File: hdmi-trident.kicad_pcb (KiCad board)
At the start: 4 copper layers, 34.5 x 48 mm, 7 parts, among them J1 HDMI_A_1.4, J2 HDMI_A_1.4, J3 Conn_02x06_Odd_Even, J4 Conn_01x06, J5 HDMI_A_1.4

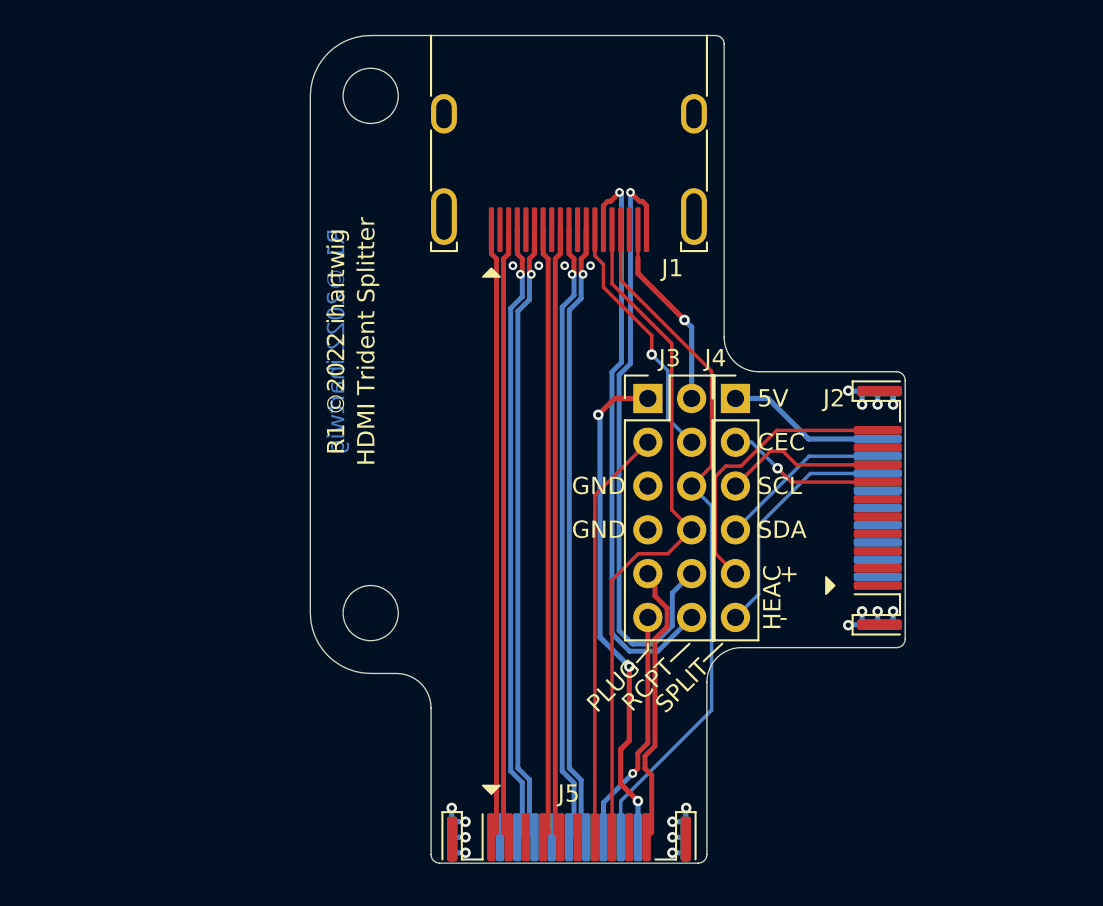
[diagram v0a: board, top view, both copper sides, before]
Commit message: change rcpt to vertical smt w/ new board shape
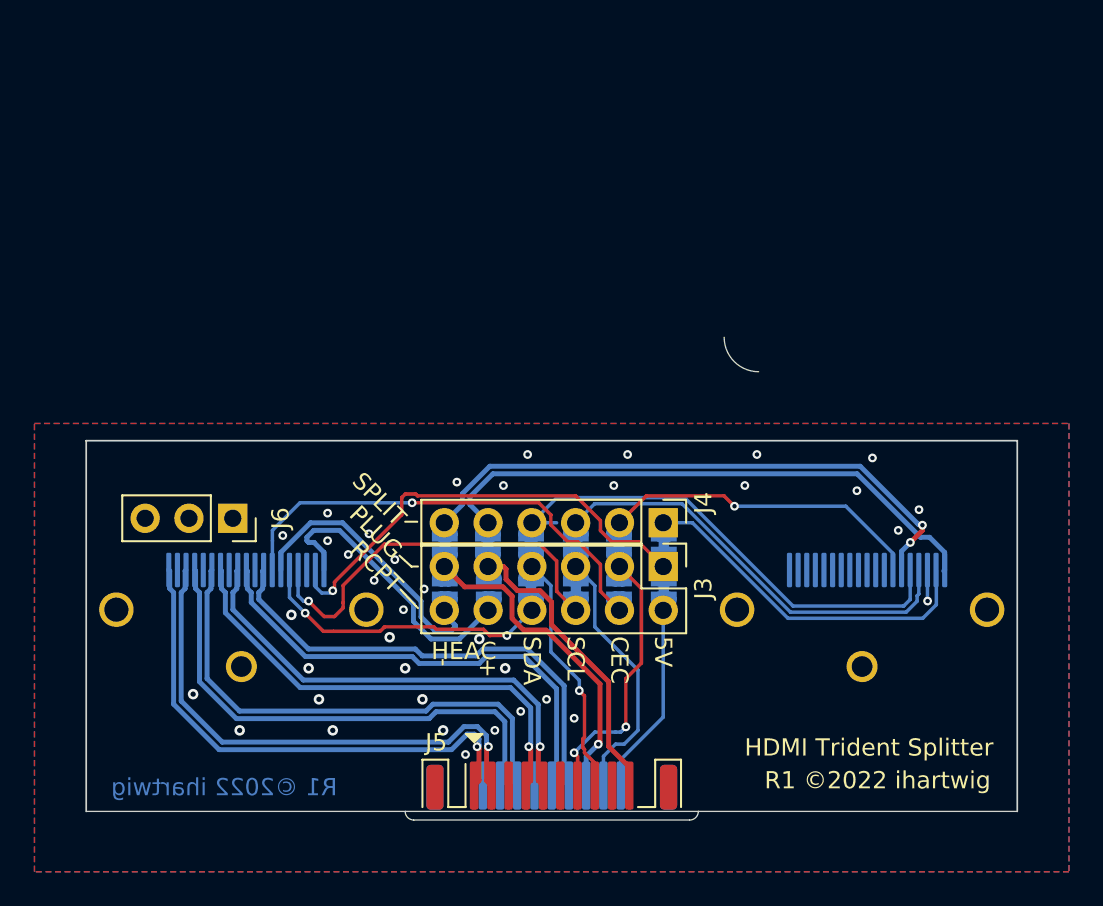
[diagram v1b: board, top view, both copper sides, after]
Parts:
- removed REF** (x2): MountingHole_3.2mm_M3_DIN965, MountingHole:MountingHole_3.2mm_M3_DIN965
- added J6: Conn_01x03, Connector_PinSocket_2.54mm:PinSocket_1x03_P2.54mm_Vertical, F.Cu at (131.5, 89.5)
- added JP1: SolderJumper_2_Bridged, Jumper:SolderJumper-2_P1.3mm_Bridged_RoundedPad1.0x1.5mm, B.Cu at (156.5, 93.6)
- added JP10: SolderJumper_2_Open, Jumper:SolderJumper-2_P1.3mm_Open_RoundedPad1.0x1.5mm, B.Cu at (151.4, 91.0)
- added JP11: SolderJumper_2_Bridged, Jumper:SolderJumper-2_P1.3mm_Bridged_RoundedPad1.0x1.5mm, B.Cu at (146.3, 91.0)
- added JP12: SolderJumper_2_Bridged, Jumper:SolderJumper-2_P1.3mm_Bridged_RoundedPad1.0x1.5mm, B.Cu at (143.8, 91.0)
- added JP2: SolderJumper_2_Open, Jumper:SolderJumper-2_P1.3mm_Open_RoundedPad1.0x1.5mm, B.Cu at (153.9, 93.6)
- added JP3: SolderJumper_2_Bridged, Jumper:SolderJumper-2_P1.3mm_Bridged_RoundedPad1.0x1.5mm, B.Cu at (151.4, 93.6)
- added JP4: SolderJumper_2_Bridged, Jumper:SolderJumper-2_P1.3mm_Bridged_RoundedPad1.0x1.5mm, B.Cu at (148.8, 93.6)
- added JP5: SolderJumper_2_Open, Jumper:SolderJumper-2_P1.3mm_Open_RoundedPad1.0x1.5mm, B.Cu at (146.3, 93.6)
- added JP6: SolderJumper_2_Open, Jumper:SolderJumper-2_P1.3mm_Open_RoundedPad1.0x1.5mm, B.Cu at (143.8, 93.6)
- added JP7: SolderJumper_2_Bridged, Jumper:SolderJumper-2_P1.3mm_Bridged_RoundedPad1.0x1.5mm, B.Cu at (156.5, 91.0)
- added JP8: SolderJumper_2_Bridged, Jumper:SolderJumper-2_P1.3mm_Bridged_RoundedPad1.0x1.5mm, B.Cu at (153.9, 91.0)
- added JP9: SolderJumper_2_Open, Jumper:SolderJumper-2_P1.3mm_Open_RoundedPad1.0x1.5mm, B.Cu at (148.8, 91.0)
- J1: footprint hdmi-trident-special:HDMI_A_Rcpt_HD04 -> hdmi-trident-special:HDMI_A_Rcpt_Vert_3Post; moved to B.Cu
- J2: footprint hdmi-trident-special:HDMI_A_Contact_Technology_HDMI-19APL2_Horizontal -> hdmi-trident-special:HDMI_A_Rcpt_Vert_3Post; moved to B.Cu
- J5: footprint hdmi-trident-special:HDMI_A_Contact_Technology_HDMI-19APL2_Horizontal -> hdmi-trident-special:HDMI_A_Plug_Horizontal_EdgeMount
- moved J1 28.0 mm to (132.0, 92.5)
- moved J3 9.79 mm to (156.5, 92.3), turned to -90 degrees
- moved J4 8.34 mm to (156.5, 89.8), turned to -90 degrees
- moved J2 3.71 mm to (168.0, 92.5), turned to 180 degrees
- moved J5 3.16 mm to (150.0, 105.0)
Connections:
- net Net-(J1-Pad13) renamed /SRC_CEC
- net Net-(J3-Pad3) renamed /SINK_CEC
- J1 pad 14: /SRC_HEAC_P -> /SINK_HEAC_P
- J1 pad 15: /DDC_SCL -> /SRC_DDC_SCL
- J1 pad 16: /DDC_SDA -> /SRC_DDC_SDA
- J1 pad 19: /SRC_HEAC_N -> /SINK_HEAC_N
- J2 pad 1: Net-(J2-Pad1) -> unconnected-(J2-Pad1)
- J2 pad 10: Net-(J2-Pad10) -> unconnected-(J2-Pad10)
- J2 pad 12: Net-(J2-Pad12) -> unconnected-(J2-Pad12)
- J2 pad 3: Net-(J2-Pad3) -> unconnected-(J2-Pad3)
- J2 pad 4: Net-(J2-Pad4) -> unconnected-(J2-Pad4)
- J2 pad 6: Net-(J2-Pad6) -> unconnected-(J2-Pad6)
- J2 pad 7: Net-(J2-Pad7) -> unconnected-(J2-Pad7)
- J2 pad 9: Net-(J2-Pad9) -> unconnected-(J2-Pad9)
- J3 pad 10: /SRC_HEAC_N -> /SINK_HEAC_N
- J3 pad 11: /SINK_HEAC_P -> /SRC_HEAC_P
- J3 pad 12: /SRC_HEAC_P -> /SINK_HEAC_P
- J3 pad 5: GND -> /SINK_DDC_SDA
- J3 pad 6: /DDC_SDA -> /SRC_DDC_SDA
- J3 pad 7: GND -> /SINK_DDC_SCL
- J3 pad 8: /DDC_SCL -> /SRC_DDC_SCL
- J3 pad 9: /SINK_HEAC_N -> /SRC_HEAC_N
- J4 pad 3: /SPLIT_DDC_SCL -> /SPLIT_DDC_SDA
- J4 pad 4: /SPLIT_DDC_SDA -> /SPLIT_DDC_SCL
- J5 pad 14: /SINK_HEAC_P -> /SRC_HEAC_P
- J5 pad 15: /DDC_SCL -> /SINK_DDC_SCL
- J5 pad 16: /DDC_SDA -> /SINK_DDC_SDA
- J5 pad 19: /SINK_HEAC_N -> /SRC_HEAC_N
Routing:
- net /DDC_SDA: track 40.6 -> 0.00 mm
- net /DDC_SCL: track 40.1 -> 0.00 mm
- net /SRC_DDC_SDA: track 0.00 -> 23.2 mm, vias 0 -> 1
- net GND: track 23.6 -> 1.80 mm, vias 20 -> 38
- net /SPLIT_HEAC_P: track 14.1 -> 34.0 mm, vias 0 -> 2
- net /SPLIT_DDC_SCL: track 9.43 -> 28.5 mm
- net /SRC_DDC_SCL: track 0.00 -> 18.4 mm, vias 0 -> 2
- net /SRC_HEAC_N: track 35.7 -> 17.4 mm, vias 1 -> 0
- net /SPLIT_HEAC_N: track 16.6 -> 33.0 mm
- net /SRC_HEAC_P: track 34.4 -> 18.8 mm
- net /SINK_DDC_SDA: track 0.00 -> 15.3 mm
- net /SPLIT_DDC_SDA: track 10.0 -> 25.0 mm
- net /SINK_DDC_SCL: track 0.00 -> 14.3 mm, vias 0 -> 1
- net /SRC_CEC: track 14.7 -> 26.9 mm
- net /SPLIT_5V: track 9.23 -> 20.5 mm
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- added copper zone on B.Cu, net GND
- added copper zone on F.Cu, net GND
- removed copper zone on In1.Cu, net GND
- removed copper zone on In2.Cu, net GND
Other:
- board size 34.5 x 48 mm -> 54 x 28 mm
- copper layers 4 -> 2
- net class 100ohm removed
- net class Default removed
- rule pad_to_mask_clearance: 0.05 -> 0.0762
- board text removed: "GND"

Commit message: cleanup graphics and add new R1 gerbers
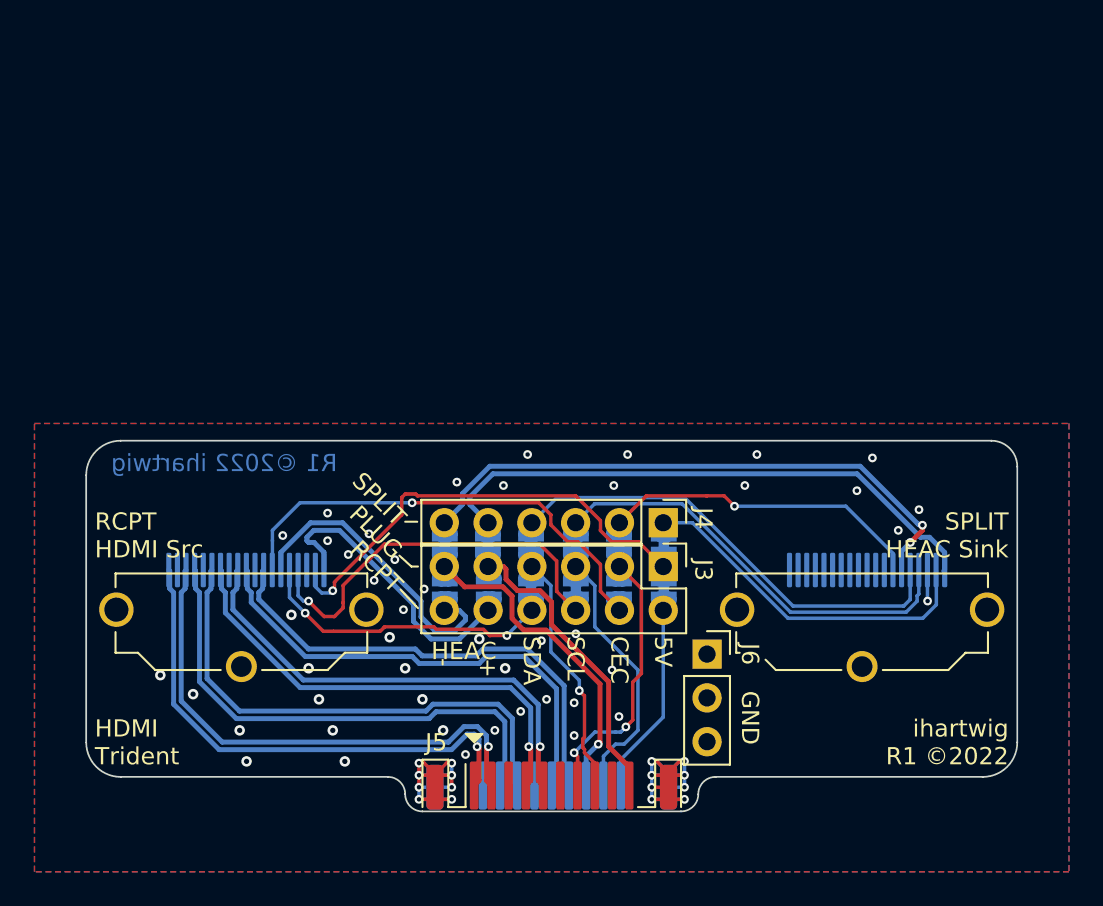
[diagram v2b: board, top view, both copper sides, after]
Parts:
- moved J6 28.6 mm to (159.0, 97.4), turned to 0 degrees
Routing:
- net GND: track 1.80 -> 44.4 mm, vias 38 -> 62
- net /SPLIT_DDC_SCL: track 28.5 -> 27.0 mm
- net /SINK_HEAC_P: track 16.3 -> 17.6 mm
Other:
- board size 54 x 28 mm -> 54 x 21.5 mm
- board text added: "GND"
- board text added: "HDMI Trident"
- board text added: "RCPT HDMI Src"
- board text added: "SPLIT HEAC Sink"
- board text added: "ihartwig R1 ©2022"
- board text removed: "HDMI Trident Splitter"
